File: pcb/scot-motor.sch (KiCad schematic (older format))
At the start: 0 parts

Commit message: WIP.
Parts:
- added J? (x7): Conn_01x02_Female, symbol Connector:Conn_01x02_Female
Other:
- note added: "0.1" Terminal Block"
- note added: "28V IN"
- note added: ">0.1" Terminal Block"
- note added: "CAN"
- note added: "ESTOP"
- note added: "LIMIT_1"
- note added: "LIMIT_2"
- note added: "MOTOR"
- note added: "TODO: Sort out global ground."
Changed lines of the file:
@@
 $EndDescr
 $Sheet
-S 1250 2650 2200 1150
+S 2000 2950 2200 1150
 U 5E55A5CD
 F0 "CAN Transceiver" 50
 F1 "scot-can-txrx.sch" 50
-F2 "CAN_L" I L 1250 3050 50
-F3 "CAN_H" I L 1250 3300 50
+F2 "CAN_L" I L 2000 3350 50
+F3 "CAN_H" I L 2000 3600 50
+F4 "CAN_MCU_RXD" I R 4200 3700 50
+F5 "CAN_MCU_TXD" I R 4200 3600 50
+F6 "3.3V_MCU" I R 4200 3050 50
+F7 "5V_CAN" I R 4200 3200 50
+F8 "LV_GND" I R 4200 3350 50
 $EndSheet
 $Sheet
-S 3850 2500 1200 1500
+S 6700 2450 1200 1500
 U 5E55A713
 F0 "MCU" 50
 F1 "scot-motor-mcu.sch" 50
+F2 "MOTOR_A" I R 7900 2600 50
+F3 "MOTOR_B" I R 7900 2700 50
+F4 "LIMIT_1A" I R 7900 2850 50
+F5 "LIMIT_1B" I R 7900 2950 50
+F6 "LIMIT_2A" I R 7900 3100 50
+F7 "LIMIT_2B" I R 7900 3200 50
+F8 "ESTOP_B" I R 7900 3500 50
+F9 "ESTOP_A" I R 7900 3400 50
+F10 "VI_I2C_SCL" I L 6700 2850 50
+F11 "VI_I2C_SDA" I L 6700 2950 50
 $EndSheet
 $Sheet
-S 4700 800  2300 1050
+S 3300 850  1650 1650
 U 5E55A987
 F0 "Power Supplies" 50
 F1 "scot-motor-power.sch" 50
+F2 "POWER_28V+" I L 3300 1000 50
+F3 "POWER_28V-" I L 3300 1100 50
+F4 "3V3_MCU" I R 4950 2200 50
+F5 "5V_CAN" I R 4950 2050 50
+F6 "MOTOR_28V-" I R 4950 1100 50
+F7 "MOTOR_28V+" I R 4950 1000 50
+F8 "VI_SDA" I R 4950 1500 50
+F9 "VI_SCL" I R 4950 1600 50
+F10 "VI_ALERT" I R 4950 1700 50
+F11 "LV_GND" I R 4950 2350 50
 $EndSheet
+$Comp
+L Connector:Conn_01x02_Female J?
+U 1 1 5E880BD6
+P 2250 1100
+F 0 "J?" H 2142 775 50  0000 C CNN
+F 1 "Conn_01x02_Female" H 2142 866 50  0000 C CNN
+F 2 "" H 2250 1100 50  0001 C CNN
+F 3 "~" H 2250 1100 50  0001 C CNN
+	1    2250 1100
+	-1   0    0    1
+$EndComp
+Text Notes 2000 1300 0    50   ~ 0
+>0.1" Terminal Block
+Text Notes 9000 2850 0    50   ~ 0
+>0.1" Terminal Block
+$Comp
+L Connector:Conn_01x02_Female J?
+U 1 1 5F16698D
+P 9500 2700
+F 0 "J?" H 9392 2375 50  0000 C CNN
+F 1 "Conn_01x02_Female" H 9392 2466 50  0000 C CNN
+F 2 "" H 9500 2700 50  0001 C CNN
+F 3 "~" H 9500 2700 50  0001 C CNN
+	1    9500 2700
+	1    0    0    1
+$EndComp
+Text Notes 9000 3600 0    50   ~ 0
+0.1" Terminal Block
+$Comp
+L Connector:Conn_01x02_Female J?
+U 1 1 5F169795
+P 9500 3450
+F 0 "J?" H 9392 3125 50  0000 C CNN
+F 1 "Conn_01x02_Female" H 9392 3216 50  0000 C CNN
+F 2 "" H 9500 3450 50  0001 C CNN
+F 3 "~" H 9500 3450 50  0001 C CNN
+	1    9500 3450
+	1    0    0    1
+$EndComp
+Text Notes 9000 4300 0    50   ~ 0
+0.1" Terminal Block
+$Comp
+L Connector:Conn_01x02_Female J?
+U 1 1 5F16A059
+P 9500 4150
+F 0 "J?" H 9392 3825 50  0000 C CNN
+F 1 "Conn_01x02_Female" H 9392 3916 50  0000 C CNN
+F 2 "" H 9500 4150 50  0001 C CNN
+F 3 "~" H 9500 4150 50  0001 C CNN
+	1    9500 4150
+	1    0    0    1
+$EndComp
+Text Notes 9000 5000 0    50   ~ 0
+0.1" Terminal Block
+$Comp
+L Connector:Conn_01x02_Female J?
+U 1 1 5F16B504
+P 9500 4850
+F 0 "J?" H 9392 4525 50  0000 C CNN
+F 1 "Conn_01x02_Female" H 9392 4616 50  0000 C CNN
+F 2 "" H 9500 4850 50  0001 C CNN
+F 3 "~" H 9500 4850 50  0001 C CNN
+	1    9500 4850
+	1    0    0    1
+$EndComp
+Text Notes 9950 2700 0    100  ~ 20
+MOTOR
+Text Notes 9950 3450 0    100  ~ 20
+LIMIT_1
+Text Notes 9950 4150 0    100  ~ 20
+LIMIT_2
+Text Notes 9950 4850 0    100  ~ 20
+ESTOP
+Text Notes 1300 1150 0    100  ~ 20
+28V IN
+$Comp
+L Connector:Conn_01x02_Female J?
+U 1 1 5F16DEFB
+P 1250 3350
+F 0 "J?" H 1142 3025 50  0000 C CNN
+F 1 "Conn_01x02_Female" H 1142 3116 50  0000 C CNN
+F 2 "" H 1250 3350 50  0001 C CNN
+F 3 "~" H 1250 3350 50  0001 C CNN
+	1    1250 3350
+	-1   0    0    1
+$EndComp
+Text Notes 600  3550 0    100  ~ 20
+CAN
+$Comp
+L Connector:Conn_01x02_Female J?
+U 1 1 5F16F7C8
+P 1250 3750
+F 0 "J?" H 1142 3425 50  0000 C CNN
+F 1 "Conn_01x02_Female" H 1142 3516 50  0000 C CNN
+F 2 "" H 1250 3750 50  0001 C CNN
+F 3 "~" H 1250 3750 50  0001 C CNN
+	1    1250 3750
+	-1   0    0    1
+$EndComp
+Text Notes 1000 3950 0    50   ~ 0
+0.1" Terminal Block
+Text Notes 4650 4650 0    50   ~ 0
+TODO: Sort out global ground.
 $EndSCHEMATC

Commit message: WIP.
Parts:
- removed J? (x2): Conn_01x02_Female, symbol Connector:Conn_01x02_Female
- added J1, J2: Conn_01x03_Female, TerminalBlock_TE-Connectivity:TerminalBlock_TE_282834-3_1x03_P2.54mm_Horizontal, symbol Connector:Conn_01x03_Female
- added JP1: SolderJumper_2_Open, Jumper:SolderJumper-2_P1.3mm_Open_RoundedPad1.0x1.5mm, symbol Jumper:SolderJumper_2_Open
- J3, J4: renamed from J?; footprint (none) -> TerminalBlock_RND:TerminalBlock_RND_205-00287_1x02_P5.08mm_Horizontal
- J5, J6, J7: renamed from J?; footprint (none) -> TerminalBlock_TE-Connectivity:TerminalBlock_TE_282834-2_1x02_P2.54mm_Horizontal
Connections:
- net CAN Transceiver/CAN_H: now also J1.3 (Pin_3), J2.3 (Pin_3)
- net CAN Transceiver/CAN_L: now also J1.2 (Pin_2), J2.2 (Pin_2)
- net MCU/ESTOP_A: now also J7.2 (Pin_2)
- net MCU/ESTOP_B: now also J7.1 (Pin_1)
- net MCU/LIMIT_1A: now also J5.2 (Pin_2)
- net MCU/LIMIT_1B: now also J5.1 (Pin_1)
- net MCU/LIMIT_2A: now also J6.2 (Pin_2)
- net MCU/LIMIT_2B: now also J6.1 (Pin_1)
- net MCU/MOTOR_A: now also J4.2 (Pin_2)
- net MCU/MOTOR_B: now also J4.1 (Pin_1)
- net Power Supplies/POWER_28V+: now also J3.2 (Pin_2)
- net GND: now reaches J3.1 (Pin_1)
- net GND: now also JP1.2 (B)
- new net: J1.1 (Pin_1), J2.1 (Pin_1), JP1.1 (A)
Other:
- note added: "0.2" Terminal Block"
- note added: "100n across Motor"
- note removed: ">0.1" Terminal Block"
- note removed: "TODO: Sort out global ground."
- moved on the sheet: J3

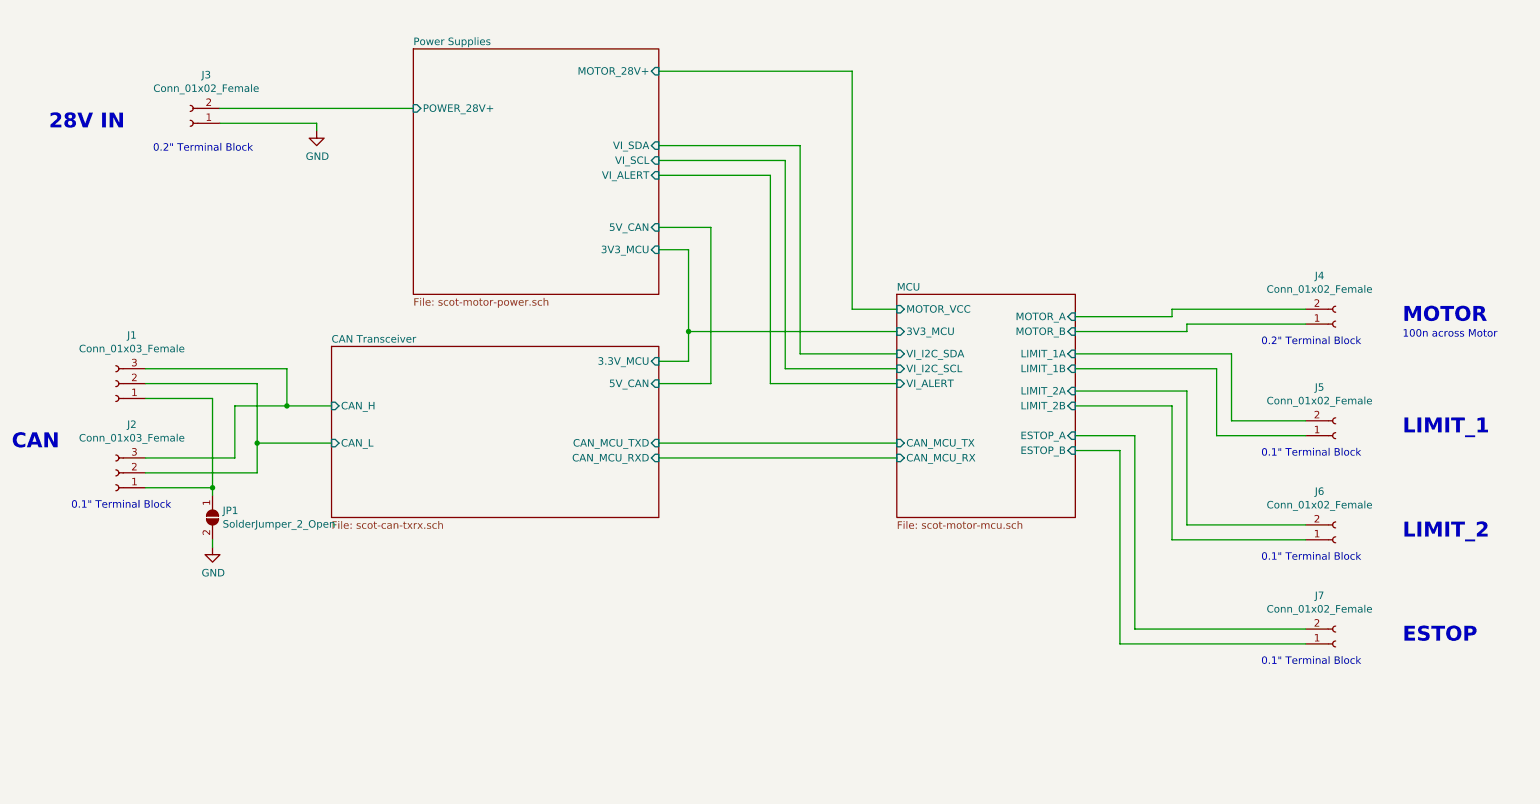
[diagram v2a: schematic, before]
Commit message: pcb: Add brake clutch driver.
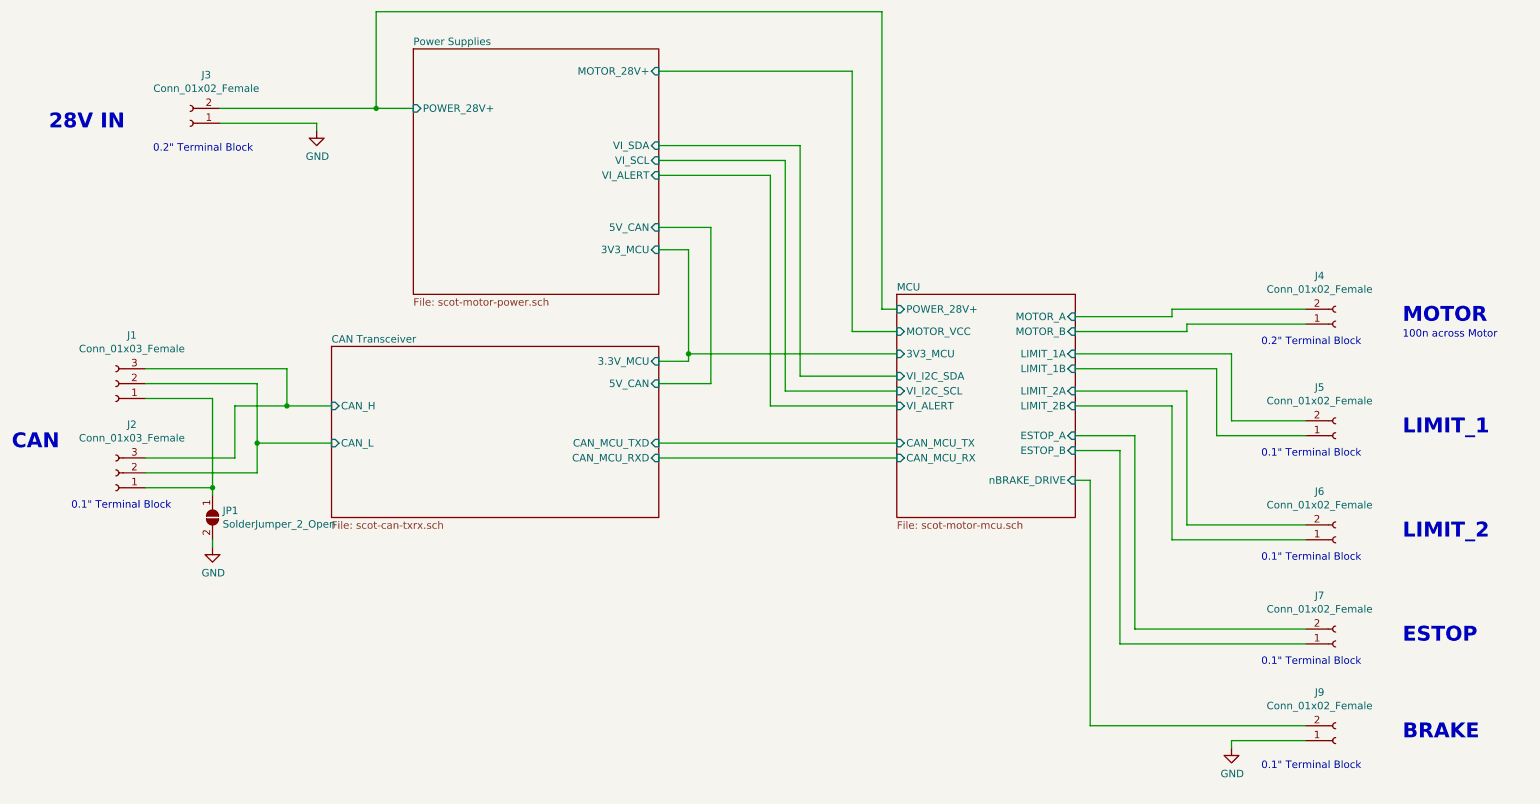
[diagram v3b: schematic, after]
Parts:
- added J9: Conn_01x02_Female, TerminalBlock_TE-Connectivity:TerminalBlock_TE_282834-2_1x02_P2.54mm_Horizontal, symbol Connector:Conn_01x02_Female
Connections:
- net GND: now also J9.1 (Pin_1)
- net Power Supplies/POWER_28V+ renamed MCU/POWER_28V+
- new net MCU/nBRAKE_DRIVE: J9.2 (Pin_2)
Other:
- note added: "BRAKE"

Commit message: PCB progress, schematic fixes.
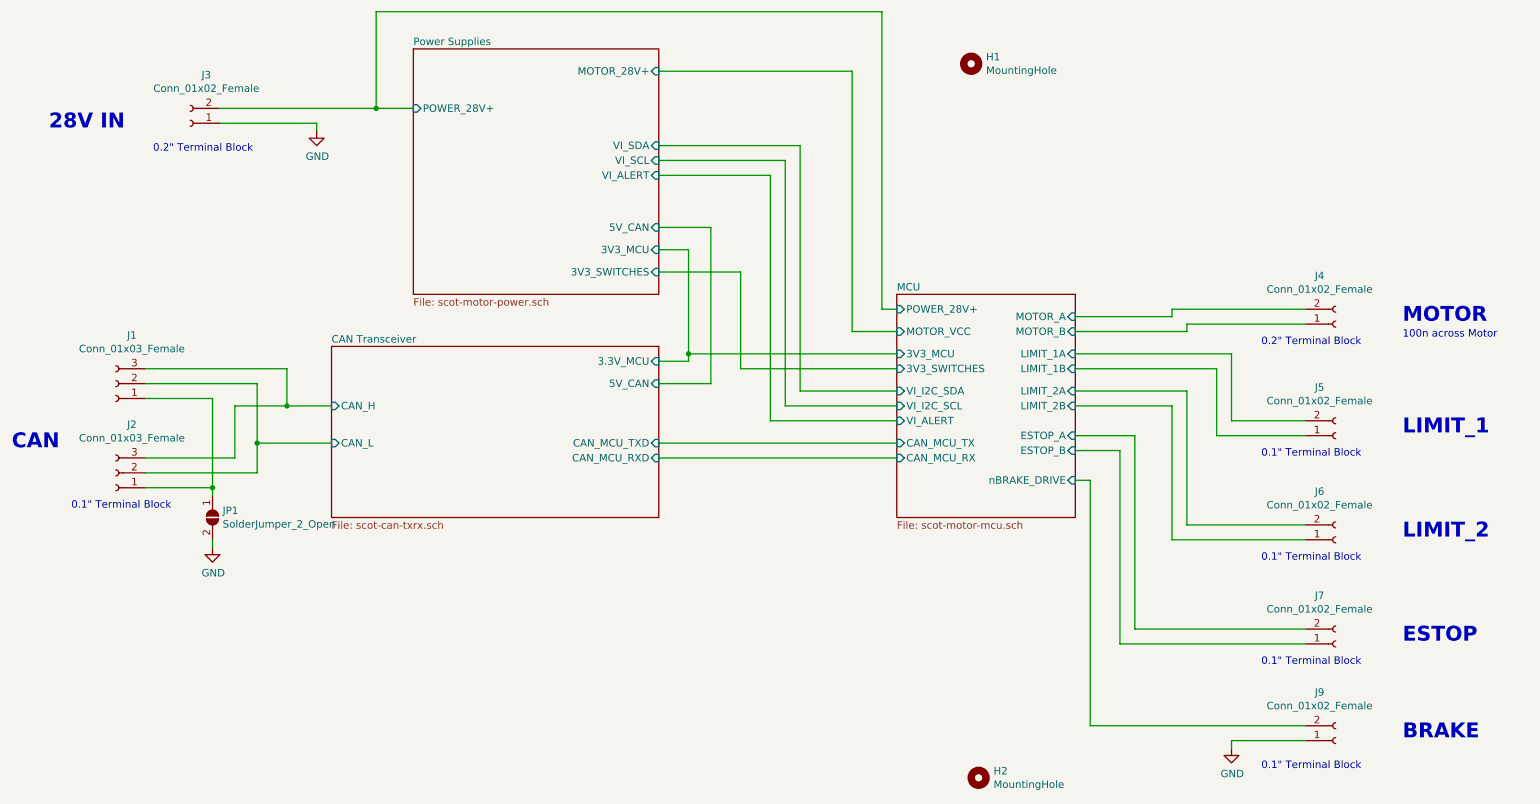
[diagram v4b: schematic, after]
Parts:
- added H1, H2: MountingHole, agg:M3_MOUNT, symbol Mechanical:MountingHole
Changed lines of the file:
@@
 F7 "VI_SCL" I R 4950 1600 50
 F8 "VI_ALERT" I R 4950 1700 50
+F9 "3V3_SWITCHES" I R 4950 2350 50
 $EndSheet
 $Comp
@@
 F8 "ESTOP_B" I R 7750 3550 50
 F9 "ESTOP_A" I R 7750 3450 50
-F10 "VI_I2C_SCL" I L 6550 3150 50
-F11 "VI_I2C_SDA" I L 6550 3050 50
+F10 "VI_I2C_SCL" I L 6550 3250 50
+F11 "VI_I2C_SDA" I L 6550 3150 50
 F12 "3V3_MCU" I L 6550 2900 50
-F13 "VI_ALERT" I L 6550 3250 50
+F13 "VI_ALERT" I L 6550 3350 50
 F14 "MOTOR_VCC" I L 6550 2750 50
 F15 "CAN_MCU_RX" I L 6550 3600 50
@@
 F17 "POWER_28V+" I L 6550 2600 50
 F18 "nBRAKE_DRIVE" I R 7750 3750 50
+F19 "3V3_SWITCHES" I L 6550 3000 50
 $EndSheet
 $Comp
@@
 	6250 1000 6250 2750
 Wire Wire Line
-	5900 3050 6550 3050
-Wire Wire Line
-	5900 1500 5900 3050
-Wire Wire Line
-	5800 3150 6550 3150
-Wire Wire Line
-	5800 1600 5800 3150
-Wire Wire Line
-	5700 3250 6550 3250
-Wire Wire Line
-	5700 1700 5700 3250
+	5900 3150 6550 3150
+Wire Wire Line
+	5900 1500 5900 3150
+Wire Wire Line
+	5800 3250 6550 3250
+Wire Wire Line
+	5800 1600 5800 3250
+Wire Wire Line
+	5700 3350 6550 3350
+Wire Wire Line
+	5700 1700 5700 3350
 Wire Wire Line
 	6550 2900 5150 2900
@@
 Wire Wire Line
 	8800 5500 9300 5500
+Wire Wire Line
+	4950 2350 5500 2350
+Wire Wire Line
+	5500 2350 5500 3000
+Wire Wire Line
+	5500 3000 6550 3000
+$Comp
+L Mechanical:MountingHole H1
+U 1 1 5E977F28
+P 7050 950
+F 0 "H1" H 7150 996 50  0000 L CNN
+F 1 "MountingHole" H 7150 905 50  0000 L CNN
+F 2 "agg:M3_MOUNT" H 7050 950 50  0001 C CNN
+F 3 "~" H 7050 950 50  0001 C CNN
+	1    7050 950
+	1    0    0    -1
+$EndComp
+$Comp
+L Mechanical:MountingHole H2
+U 1 1 5E97838F
+P 7100 5750
+F 0 "H2" H 7200 5796 50  0000 L CNN
+F 1 "MountingHole" H 7200 5705 50  0000 L CNN
+F 2 "agg:M3_MOUNT" H 7100 5750 50  0001 C CNN
+F 3 "~" H 7100 5750 50  0001 C CNN
+	1    7100 5750
+	1    0    0    -1
+$EndComp
 $EndSCHEMATC

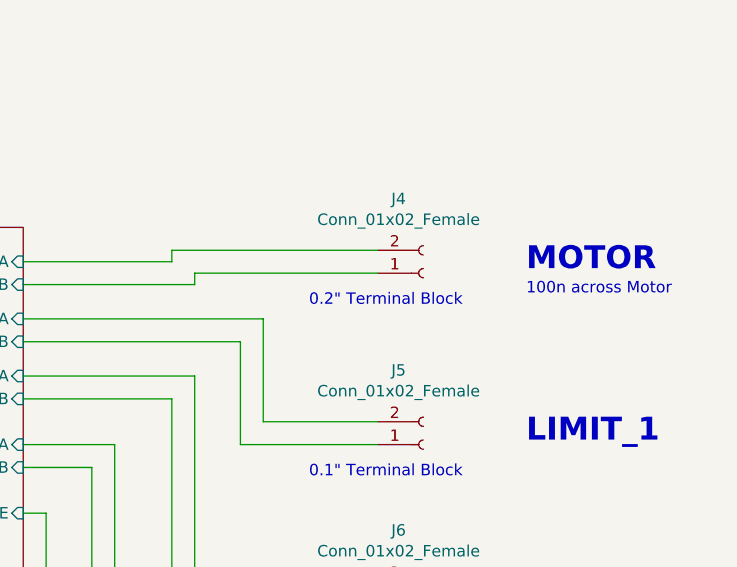
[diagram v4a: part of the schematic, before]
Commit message: pcb: Add ground terminal on motor terminal block for shielding.
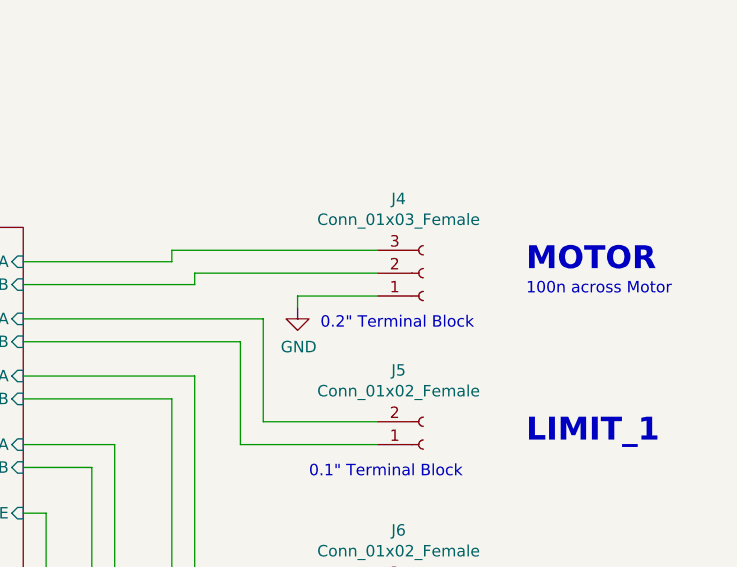
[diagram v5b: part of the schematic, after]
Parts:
- removed J4: Conn_01x02_Female, TerminalBlock_RND:TerminalBlock_RND_205-00287_1x02_P5.08mm_Horizontal, symbol Connector:Conn_01x02_Female
- added J4: Conn_01x03_Female, TerminalBlock_RND:TerminalBlock_RND_205-00288_1x03_P5.08mm_Horizontal, symbol Connector:Conn_01x03_Female
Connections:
- net GND: now also J4.1 (Pin_1)
- net MCU/MOTOR_A: now also J4.3 (Pin_3)
- net MCU/MOTOR_B: now also J4.2 (Pin_2)
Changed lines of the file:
@@
 Text Notes 1550 1550 0    50   ~ 0
 0.2" Terminal Block
-Text Notes 9000 2850 0    50   ~ 0
+Text Notes 9050 2950 0    50   ~ 0
 0.2" Terminal Block
-$Comp
-L Connector:Conn_01x02_Female J4
-U 1 1 5F16698D
-P 9500 2700
-F 0 "J4" H 9392 2375 50  0000 C CNN
-F 1 "Conn_01x02_Female" H 9392 2466 50  0000 C CNN
-F 2 "TerminalBlock_RND:TerminalBlock_RND_205-00287_1x02_P5.08mm_Horizontal" H 9500 2700 50  0001 C CNN
-F 3 "~" H 9500 2700 50  0001 C CNN
-	1    9500 2700
-	1    0    0    1
-$EndComp
 Text Notes 9000 3600 0    50   ~ 0
 0.1" Terminal Block
@@
 	1    0    0    -1
 $EndComp
+$Comp
+L Connector:Conn_01x03_Female J4
+U 1 1 5EA317F2
+P 9500 2700
+F 0 "J4" H 9392 2375 50  0000 C CNN
+F 1 "Conn_01x03_Female" H 9392 2466 50  0000 C CNN
+F 2 "TerminalBlock_RND:TerminalBlock_RND_205-00288_1x03_P5.08mm_Horizontal" H 9500 2700 50  0001 C CNN
+F 3 "~" H 9500 2700 50  0001 C CNN
+	1    9500 2700
+	1    0    0    1
+$EndComp
+$Comp
+L power:GND #PWR0105
+U 1 1 5EA3B44A
+P 8950 2850
+F 0 "#PWR0105" H 8950 2600 50  0001 C CNN
+F 1 "GND" H 8955 2677 50  0000 C CNN
+F 2 "" H 8950 2850 50  0001 C CNN
+F 3 "" H 8950 2850 50  0001 C CNN
+	1    8950 2850
+	1    0    0    -1
+$EndComp
+Wire Wire Line
+	9300 2800 8950 2800
+Wire Wire Line
+	8950 2800 8950 2850
 $EndSCHEMATC
